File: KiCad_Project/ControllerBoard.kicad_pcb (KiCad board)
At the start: 2 copper layers, 26.2 x 43.2 mm, 32 parts, among them J1 Main Header, J2 SWD, J3 WD_Disable, Q1 BSS84, U1 FS32K116, U2 UJA1075A

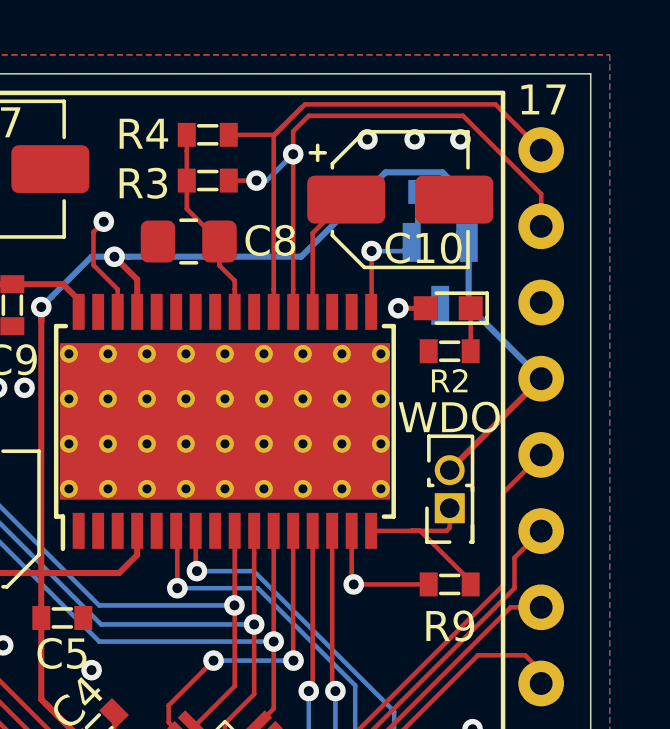
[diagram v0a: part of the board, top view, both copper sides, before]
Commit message: Drove LIMP LED directly from pin instead of from a FET
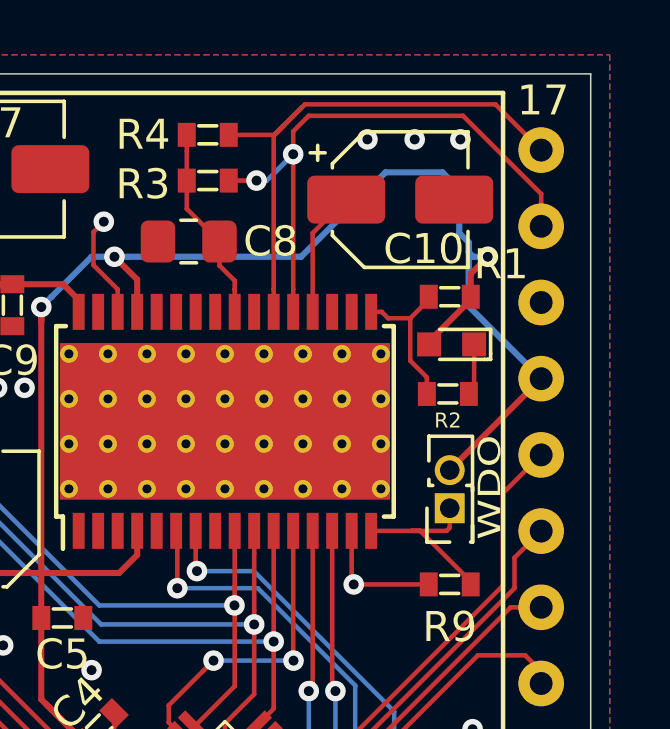
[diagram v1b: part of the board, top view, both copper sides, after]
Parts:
- removed Q1: BSS84, digikey-footprints:SOT-23-3
- D1: value LED -> LEDR
- D2, D3, D5: value LED -> LEDG
- R1: moved to F.Cu
- moved R1 3.51 mm to (139.4, 81.1)
- moved R2 1.42 mm to (139.4, 84.3)
- moved D1 1.21 mm to (139.5, 82.7)
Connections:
- D1 pad 2: Net-(D1-Pad2) -> +5V
- R2 pad 2: GND -> LIMP
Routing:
- net +5V: track 91.3 -> 96.1 mm, vias 5 -> 6
- net Net-(D1-Pad2): track 2.35 -> 0.00 mm, vias 1 -> 0
- net LIMP: track 5.25 -> 5.11 mm, vias 1 -> 0

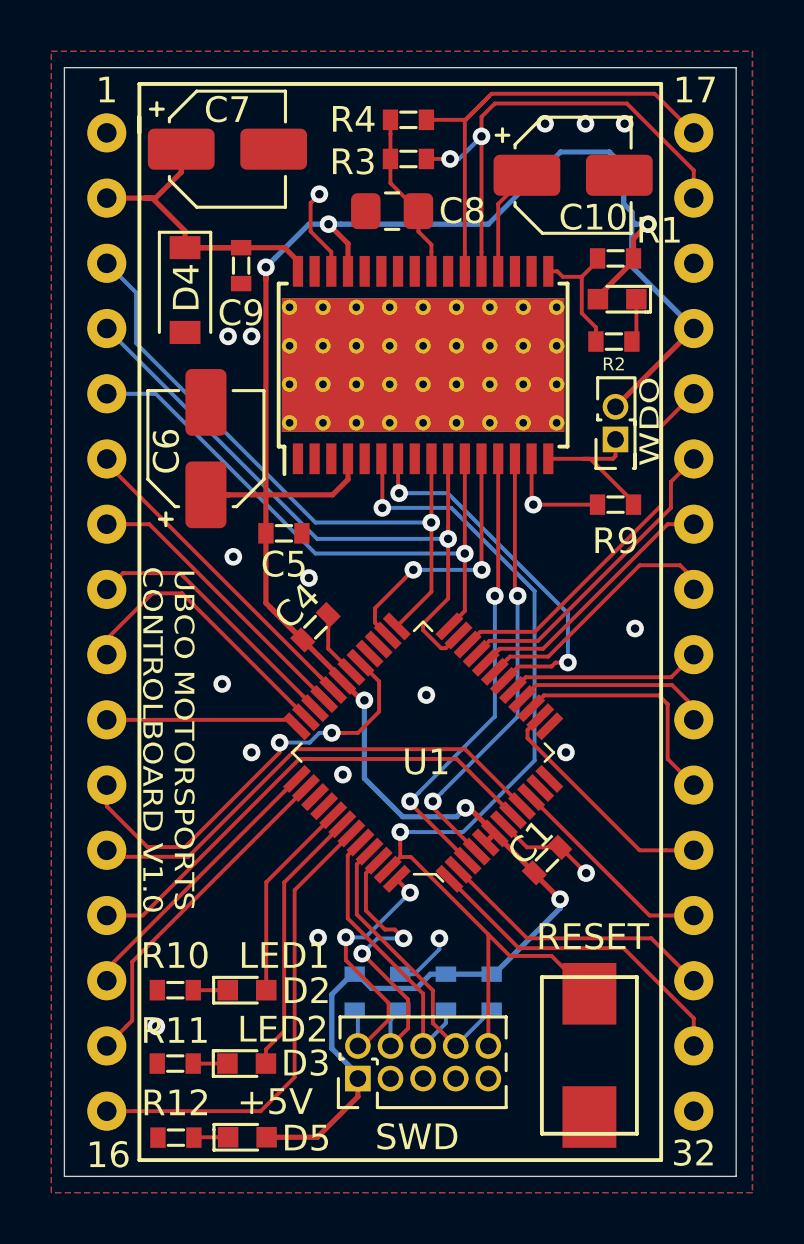
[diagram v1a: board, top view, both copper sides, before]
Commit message: Added a reset LED
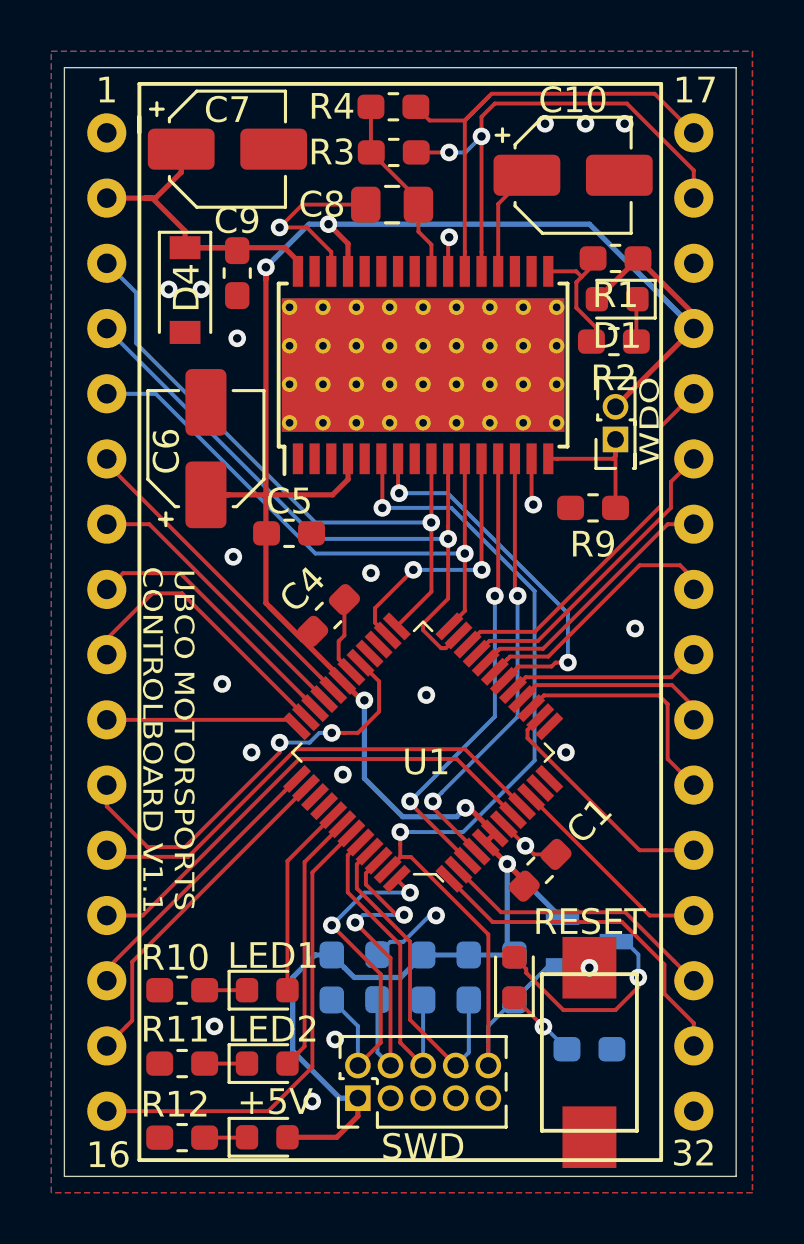
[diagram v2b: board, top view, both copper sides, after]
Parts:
- added D6: LEDR, LED_SMD:LED_0603_1608Metric, F.Cu at (135.5, 109.1)
- added Q1: BSS84, digikey-footprints:SOT-23-3, B.Cu at (138.4, 107.7)
- added R13: 10k, Resistor_SMD:R_0603_1608Metric_Pad1.05x0.95mm_HandSolder, B.Cu at (135.5, 109.1)
- added R14: 220, Resistor_SMD:R_0603_1608Metric_Pad1.05x0.95mm_HandSolder, B.Cu at (138.4, 111.9)
- C1, C4, C5, C9: footprint digikey-footprints:0603 -> Capacitor_SMD:C_0603_1608Metric_Pad1.05x0.95mm_HandSolder
- C10: value 4.7u -> 10u
- C6, C7: value 22u -> 10u
- D1, D2, D3, D5: footprint digikey-footprints:LED_0603 -> LED_SMD:LED_0603_1608Metric
- R1, R10, R11, R12, R3, R4, R5, R6, R7, R8, R9: footprint digikey-footprints:0603 -> Resistor_SMD:R_0603_1608Metric_Pad1.05x0.95mm_HandSolder
- R2: value 300 -> 220; footprint digikey-footprints:0603 -> Resistor_SMD:R_0603_1608Metric_Pad1.05x0.95mm_HandSolder
- moved R8 1.07 mm to (130.2, 109.1)
- moved R5 1.06 mm to (133.7, 109.1)
- moved R6 1.06 mm to (132.0, 109.1)
- moved R7 1.06 mm to (128.4, 109.1)
- moved R9 0.88 mm to (138.6, 90.8)
- moved D3 0.80 mm to (125.9, 112.4)
- moved D2 0.79 mm to (125.9, 109.6)
- moved R4 0.78 mm to (130.8, 75.2)
- moved D5 0.77 mm to (125.9, 115.3)
- moved J2 0.76 mm to (129.4, 113.8)
- moved C4 0.68 mm to (128.3, 95.0)
- moved R3 0.63 mm to (130.8, 77.0)
- moved C1 0.48 mm to (136.5, 104.9)
- moved C9 0.33 mm to (124.7, 81.7)
- moved R11 0.27 mm to (122.6, 112.4)
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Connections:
- S1 pad 1: GND -> RESET
- S1 pad 2: RESET -> GND
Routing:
- net Net-(D6-Pad2): track 0.00 -> 8.47 mm, vias 0 -> 1
- net +5V: track 96.1 -> 101.6 mm, vias 6 -> 5
- net RESET: track 37.8 -> 41.3 mm, vias 2 -> 3
- net SWDIO: track 10.9 -> 13.9 mm
- net Net-(D6-Pad1): track 0.00 -> 2.88 mm, vias 0 -> 1
- net GND: track 16.8 -> 19.3 mm, vias 19 -> 22
- net SWDCLK: track 12.1 -> 14.1 mm
- net SWO: track 11.1 -> 12.7 mm
- net TDI: track 11.3 -> 12.9 mm
- net SPLIT: track 6.56 -> 7.38 mm
- net CANL: track 19.1 -> 19.7 mm
- net CANH: track 20.0 -> 19.5 mm
- net PTD1: track 12.8 -> 13.4 mm
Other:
- board text added: "LV 1/2020"
- board text added: "UBCO MOTORSPORTS CONTROLBOARD V1.1"
- board text removed: "LV 10/2019"
- board text removed: "UBCO MOTORSPORTS CONTROLBOARD V1.0"
